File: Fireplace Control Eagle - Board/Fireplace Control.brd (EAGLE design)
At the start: 45.4 x 44.4 mm, 11 parts, among them IC2 MEGA8-PU, J1 POWER_JACKPTH, K1 AQV21SOP

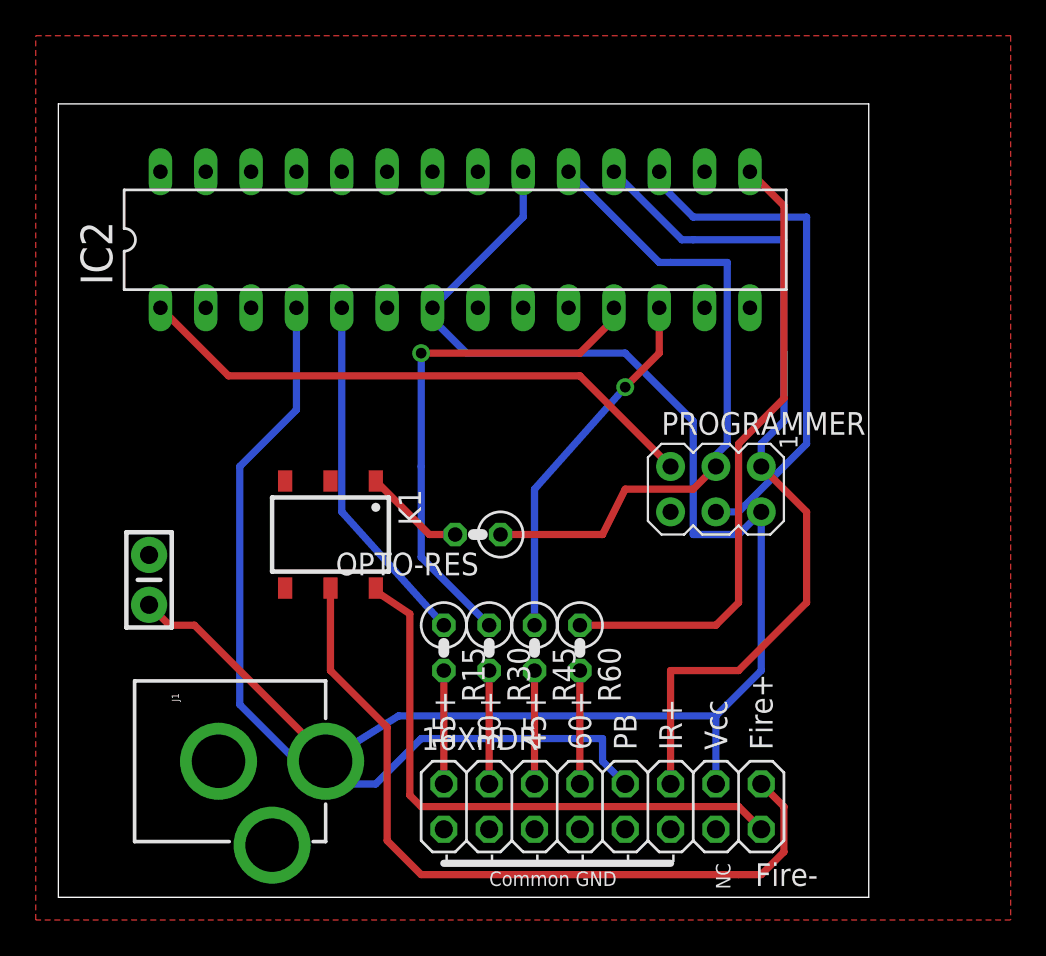
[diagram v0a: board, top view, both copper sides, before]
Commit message: Submitted to OSHPark
This is the design that went to OSHPark for productions
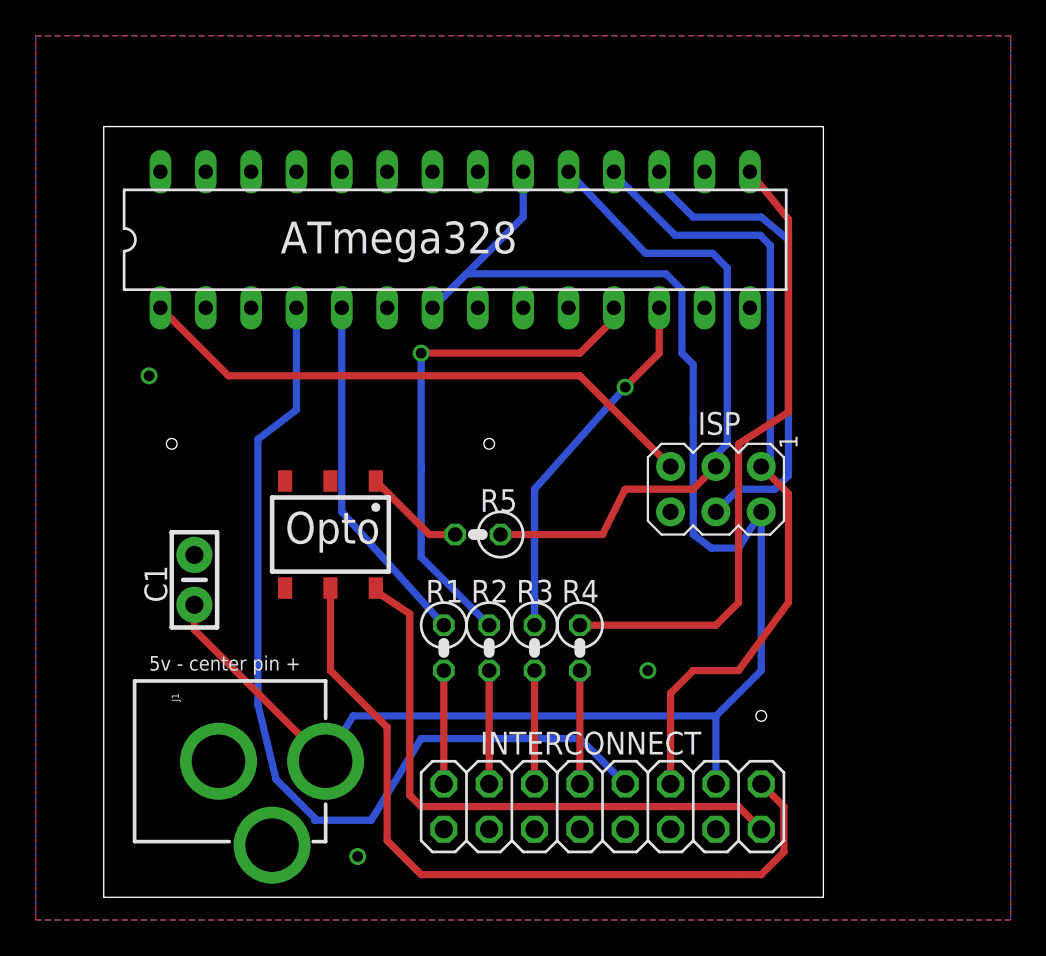
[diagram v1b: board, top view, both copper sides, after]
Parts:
- moved CAP1 2.54 mm to (7.62, 17.8)
- renumbered 16XHDR to INTERCONNECT, IC2 to 328, PROGRAMMER to ISP
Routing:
- net N$12: track 53.6 -> 45.5 mm
- net VCC: track 90.6 -> 96.0 mm
- net N$19: track 49.8 -> 51.8 mm
- net N$10: track 29.0 -> 27.2 mm
- added copper zone on layer 16, net GND
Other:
- board size 45.4 x 44.4 mm -> 40.3 x 43.2 mm
- board text added: "5v - center pin +"
- board text added: "ATmega328"
- board text added: "C1"
- board text added: "Dave Orth - 2013 - Rev A"
- board text added: "Opto"
- board text added: "PB+"
- board text added: "R1"
- board text added: "R2"
- board text added: "R3"
- board text added: "R4"
- board text added: "R5"
- board text added: "Remote Control Fireplace Board"
- board text added: "fire+"
- board text added: "fire-"
- board text added: "nc"
- board text removed: "Fire+"
- board text removed: "Fire-"
- board text removed: "NC"
- board text removed: "PB"

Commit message: First cut v2 Board
Rewired led60 to use pin 11 (instead of 9). Re-routed using FreeRoute
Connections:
- removed net N$10: 328.17, ISP.4
- net N$8: now also 328.17, ISP.4; no longer 328.15
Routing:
- net N$10: track 27.2 -> 0.00 mm
- net N$13: track 43.2 -> 30.7 mm
- net VCC: track 96.0 -> 83.6 mm
- net N$19: track 51.8 -> 42.3 mm
- net N$1: track 29.0 -> 20.7 mm, vias 1 -> 0
- net N$8: track 35.8 -> 30.6 mm
- net N$6: track 33.1 -> 28.8 mm
- net N$12: track 45.5 -> 44.3 mm
- net N$11: track 36.7 -> 35.5 mm
- net N$9: track 5.69 -> 6.25 mm
- net N$7: track 20.5 -> 20.7 mm, vias 1 -> 0
